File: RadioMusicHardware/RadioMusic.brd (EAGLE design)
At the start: 99 x 19.1 mm, 24 parts, among them IC1 TL074P, IC2 7805L, U1 USD-SOCKETNEW

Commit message: Output circuitry
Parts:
- added C3, C6: 1n, TomW:C050-024X044
- added C7, C8: 100n, TomW:C050-025X075
- added R3, R5, R6: 8.2k, TomW:0207/10
- added R4: 220R, TomW:0207/10
- added R7: 1k, TomW:0207/10
- added R8: 3.3K, TomW:0207/10
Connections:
- new net DAC: C8.2, U$1.RESET
- new net N$10: C8.1, R5.1
- new net N$2: C6.1, IC1.10, R3.2
- new net N$4: C3.2, R3.1, R5.2
- new net N$5: C3.1, C7.2, IC1.8, IC1.9
- new net N$6: C7.1, IC1.12, R6.2
- new net N$7: IC1.13, R7.2, R8.1
- new net N$8: IC1.14, R4.1, R8.2
- new net N$9: OUT1.P$3, R4.2
- net GND: now also C6.2, OUT1.P$1, R6.1, R7.1
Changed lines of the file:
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@@
 <layer number="97" name="Info" color="7" fill="1" visible="no" active="no"/>
 <layer number="98" name="Guide" color="6" fill="1" visible="no" active="no"/>
+<layer number="99" name="SpiceOrder" color="5" fill="1" visible="no" active="no"/>
 <layer number="100" name="Muster" color="7" fill="1" visible="no" active="no"/>
 <layer number="101" name="Patch_Top" color="12" fill="4" visible="yes" active="yes"/>
@@
 <element name="D1" library="diode" package="DO34-7" value="BAT81" x="4.445" y="-15.24"/>
 <element name="D2" library="diode" package="DO34-7" value="BAT81" x="4.445" y="-21.59"/>
+<element name="R3" library="TomW" package="0207/10" value="8.2k" x="4.445" y="-26.035"/>
+<element name="R4" library="TomW" package="0207/10" value="220R" x="4.445" y="-29.845"/>
+<element name="R5" library="TomW" package="0207/10" value="8.2k" x="4.445" y="-33.655"/>
+<element name="C3" library="TomW" package="C050-024X044" value="1n" x="1.905" y="-37.465"/>
+<element name="C6" library="TomW" package="C050-024X044" value="1n" x="1.905" y="-41.275"/>
+<element name="C7" library="TomW" package="C050-025X075" value="100n" x="2.54" y="-44.45"/>
+<element name="R6" library="TomW" package="0207/10" value="8.2k" x="4.445" y="-47.625"/>
+<element name="R7" library="TomW" package="0207/10" value="1k" x="4.445" y="-51.435"/>
+<element name="R8" library="TomW" package="0207/10" value="3.3K" x="4.445" y="-55.245"/>
+<element name="C8" library="TomW" package="C050-025X075" value="100n" x="2.54" y="-59.055"/>
 </elements>
 <signals>
@@
 <contactref element="D2" pad="A"/>
 <contactref element="CHANNEL" pad="1"/>
+<contactref element="OUT1" pad="P$1"/>
+<contactref element="C6" pad="2"/>
+<contactref element="R6" pad="1"/>
+<contactref element="R7" pad="1"/>
 <wire x1="92.075" y1="10.795" x2="94.615" y2="10.795" width="0" layer="19" extent="1-1"/>
 <wire x1="94.615" y1="8.255" x2="94.615" y2="10.795" width="0" layer="19" extent="1-1"/>
@@
 <wire x1="37.45" y1="6.39" x2="42.545" y2="9.525" width="0" layer="19" extent="1-1"/>
 <wire x1="27.435" y1="5.08" x2="37.45" y2="6.39" width="0" layer="19" extent="1-1"/>
-<wire x1="-0.635" y1="-10.16" x2="27.435" y2="5.08" width="0" layer="19" extent="1-1"/>
+<wire x1="12.83" y1="5.08" x2="27.435" y2="5.08" width="0" layer="19" extent="1-1"/>
+<wire x1="-0.635" y1="-10.16" x2="12.83" y2="5.08" width="0" layer="19" extent="1-1"/>
 <wire x1="8.255" y1="-21.59" x2="-0.635" y2="-10.16" width="0" layer="19" extent="1-1"/>
+<wire x1="4.445" y1="-41.275" x2="8.255" y2="-21.59" width="0" layer="19" extent="1-1"/>
+<wire x1="-0.635" y1="-47.625" x2="4.445" y2="-41.275" width="0" layer="19" extent="1-1"/>
+<wire x1="-0.635" y1="-51.435" x2="-0.635" y2="-47.625" width="0" layer="19" extent="1-1"/>
 </signal>
 <signal name="+12V" class="1">
@@
 <wire x1="37.45" y1="8.89" x2="67.945" y2="1.905" width="0" layer="19" extent="1-1"/>
 </signal>
+<signal name="DAC">
+<contactref element="U$1" pad="RESET"/>
+<contactref element="C8" pad="2"/>
+<wire x1="42.545" y1="4.445" x2="5.08" y2="-59.055" width="0" layer="19" extent="1-1"/>
+</signal>
+<signal name="N$2">
+<contactref element="IC1" pad="10"/>
+<contactref element="R3" pad="2"/>
+<contactref element="C6" pad="1"/>
+<wire x1="9.525" y1="-26.035" x2="29.845" y2="24.765" width="0" layer="19" extent="1-1"/>
+<wire x1="-0.635" y1="-41.275" x2="9.525" y2="-26.035" width="0" layer="19" extent="1-1"/>
+</signal>
+<signal name="N$4">
+<contactref element="R3" pad="1"/>
+<contactref element="R5" pad="2"/>
+<contactref element="C3" pad="2"/>
+<wire x1="9.525" y1="-33.655" x2="4.445" y2="-37.465" width="0" layer="19" extent="1-1"/>
+<wire x1="-0.635" y1="-26.035" x2="4.445" y2="-37.465" width="0" layer="19" extent="1-1"/>
+</signal>
+<signal name="N$5">
+<contactref element="C3" pad="1"/>
+<contactref element="IC1" pad="8"/>
+<contactref element="IC1" pad="9"/>
+<contactref element="C7" pad="2"/>
+<wire x1="24.765" y1="24.765" x2="27.305" y2="24.765" width="0" layer="19" extent="1-1"/>
+<wire x1="-0.635" y1="-37.465" x2="24.765" y2="24.765" width="0" layer="19" extent="1-1"/>
+<wire x1="5.08" y1="-44.45" x2="-0.635" y2="-37.465" width="0" layer="19" extent="1-1"/>
+</signal>
+<signal name="N$6">
+<contactref element="C7" pad="1"/>
+<contactref element="IC1" pad="12"/>
+<contactref element="R6" pad="2"/>
+<wire x1="9.525" y1="-47.625" x2="34.925" y2="24.765" width="0" layer="19" extent="1-1"/>
+<wire x1="0" y1="-44.45" x2="9.525" y2="-47.625" width="0" layer="19" extent="1-1"/>
+</signal>
+<signal name="N$7">
+<contactref element="IC1" pad="13"/>
+<contactref element="R7" pad="2"/>
+<contactref element="R8" pad="1"/>
+<wire x1="9.525" y1="-51.435" x2="37.465" y2="24.765" width="0" layer="19" extent="1-1"/>
+<wire x1="-0.635" y1="-55.245" x2="9.525" y2="-51.435" width="0" layer="19" extent="1-1"/>
+</signal>
+<signal name="N$8">
+<contactref element="IC1" pad="14"/>
+<contactref element="R4" pad="1"/>
+<contactref element="R8" pad="2"/>
+<wire x1="-0.635" y1="-29.845" x2="40.005" y2="24.765" width="0" layer="19" extent="1-1"/>
+<wire x1="9.525" y1="-55.245" x2="-0.635" y2="-29.845" width="0" layer="19" extent="1-1"/>
+</signal>
+<signal name="N$9">
+<contactref element="R4" pad="2"/>
+<contactref element="OUT1" pad="P$3"/>
+<wire x1="1.51" y1="5.08" x2="9.525" y2="-29.845" width="0" layer="19" extent="1-1"/>
+</signal>
+<signal name="N$10">
+<contactref element="R5" pad="1"/>
+<contactref element="C8" pad="1"/>
+<wire x1="-0.635" y1="-33.655" x2="0" y2="-59.055" width="0" layer="19" extent="1-1"/>
+</signal>
 </signals>

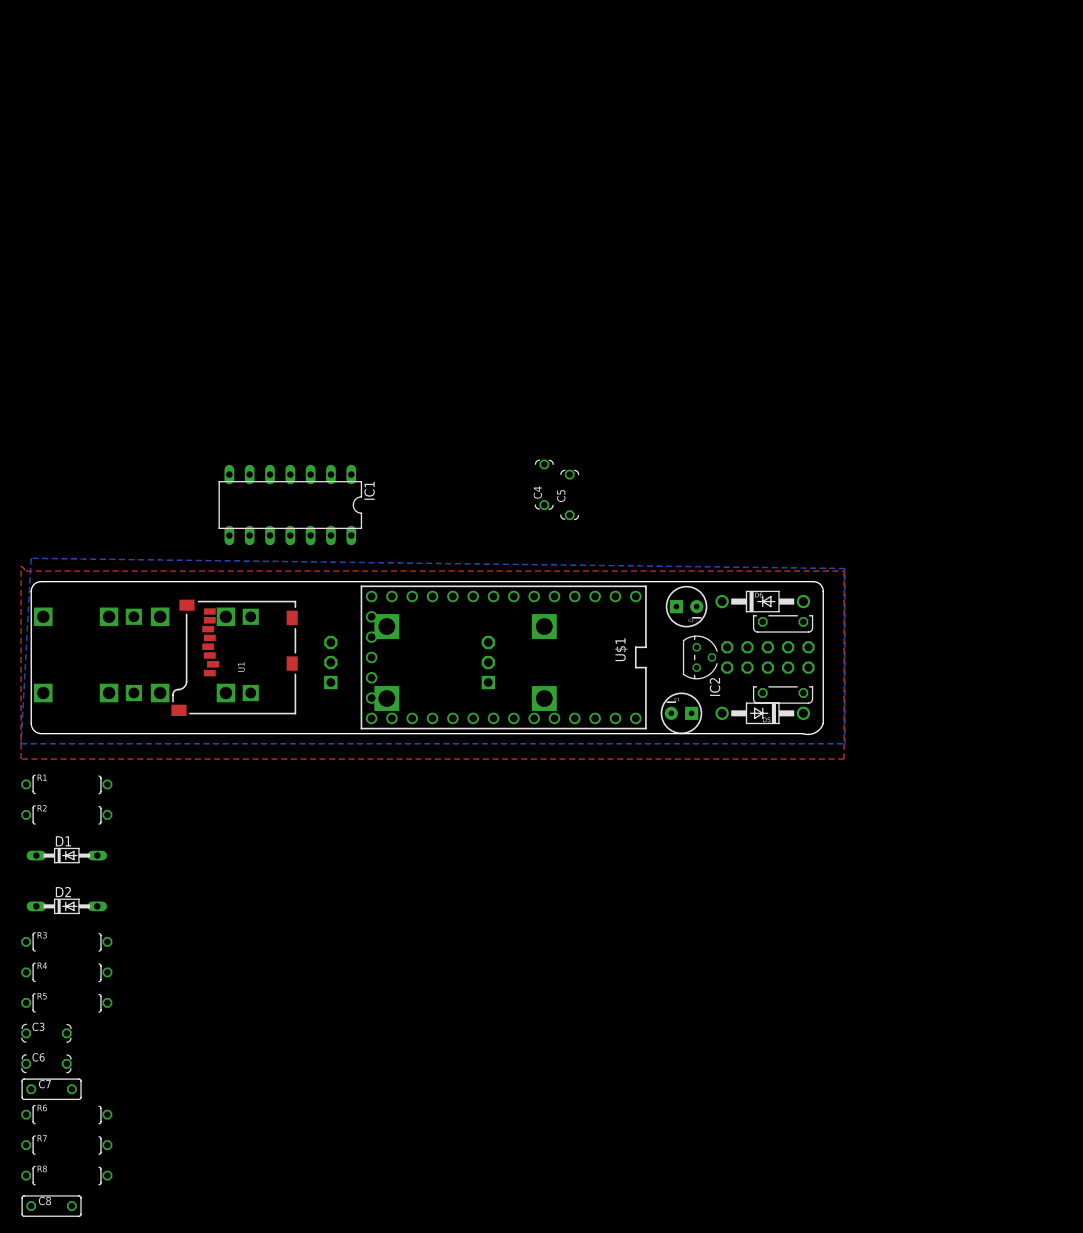
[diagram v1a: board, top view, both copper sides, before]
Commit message: Basic hardware schematic complete
Only needs SD connections & checking
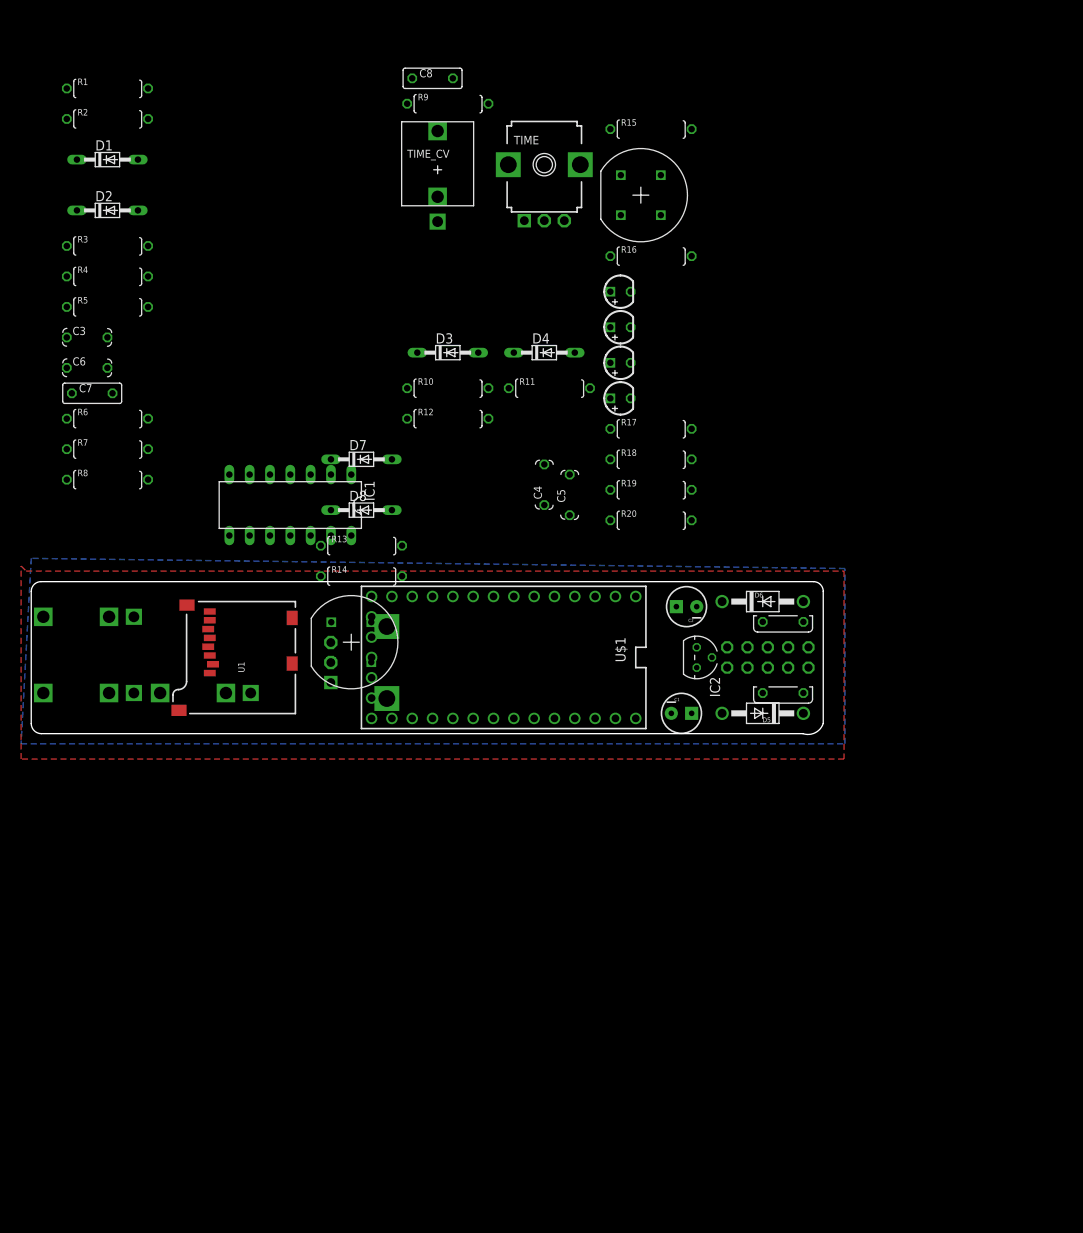
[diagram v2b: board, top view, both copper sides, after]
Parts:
- removed CV2: THONKICONN, TomW:THONKICONN
- removed GAIN1: 50k, TomW:EVUF
- added BANK_BUTTON, RESET_BUTTON: (no value), TomW:D6_BUTTON_RND
- added D3, D4, D7, D8: BAT81, diode:DO34-7
- added LED1, LED2, LED3, LED4: (no value), TomW:LED3MM
- added R10, R13: 100k, TomW:0207/10
- added R11: 200k, TomW:0207/10
- added R12, R9: 47R, TomW:0207/10
- added R14: 220R, TomW:0207/10
- added R15, R16: 10k, TomW:0207/10
- added R17, R18, R19, R20: 1k, TomW:0207/10
- added TIME: 50k, TomW:EVUF
- added TIME_CV: THONKICONN, TomW:THONKICONN
- R1: value 10k -> 100k
- R2: value 10k -> 200k
- moved C8 148.8 mm to (50.2, 81.9)
- moved C3 87.1 mm to (6.99, 49.5)
- moved C6 87.1 mm to (6.99, 45.7)
- moved C7 87.1 mm to (7.62, 42.5)
- moved D2 87.1 mm to (9.53, 65.4)
- moved R3 87.1 mm to (9.53, 61.0)
- moved R4 87.1 mm to (9.53, 57.1)
- moved R5 87.1 mm to (9.53, 53.3)
- moved R6 87.1 mm to (9.53, 39.4)
- moved R7 87.1 mm to (9.53, 35.6)
- moved R8 87.1 mm to (9.53, 31.8)
- moved D1 87.1 mm to (9.53, 71.8)
- moved R1 87.1 mm to (9.53, 80.6)
- moved R2 87.1 mm to (9.53, 76.8)
- renumbered OUT2 to RESET
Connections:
- new net N$11: R10.1, R11.2, TIME_CV.P$3
- new net N$12: IC1.5, R10.2
- new net N$13: LED1.A, U$1.3
- new net N$14: R14.1, RESET.P$3
- new net N$15: LED2.A, U$1.4
- new net N$16: LED3.A, U$1.5
- new net N$17: LED4.A, U$1.6
- new net N$18: LED1.K, R17.2
- new net N$19: LED2.K, R18.2
- new net N$20: LED3.K, R19.2
- new net N$21: LED4.K, R20.2
- new net PIN2: BANK_BUTTON.P$1, BANK_BUTTON.P$2, R15.2, U$1.2
- new net PIN20/A6: D3.A, D4.C, R12.2, U$1.20/A6
- new net PIN21/A7: TIME.2, U$1.21/A7
- new net PIN8: R16.2, RESET_BUTTON.P$1, RESET_BUTTON.P$2, U$1.8
- new net PIN9: D7.A, D8.C, R13.2, R14.2, U$1.9
- net +3.3V: now also BANK_BUTTON.P$3, BANK_BUTTON.P$4, D3.C, D7.C, RESET_BUTTON.P$3, RESET_BUTTON.P$4, TIME.3
- net GND: now also D4.A, D8.A, R11.1, R13.1, R15.1, R16.1, R17.1, R18.1, R19.1, R20.1, RESET.P$1, TIME.1, TIME_CV.P$1, U1.CD1, U1.CD2, U1.GND1, U1.GND3
- net PIN22/A8: now also IC1.6, IC1.7, R12.1, R9.1, R9.2

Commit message: Starting PCB layout
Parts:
- removed U1: USD-SOCKETNEW, SparkFun-Connectors:MICRO-SD-SOCKET-PP
- added L1, L2: BL01RN1A, inductors:BL01RN1A
- added U$3: VERT_SD_CARD, TomW:VERT_MICROSD
- BANK_BUTTON, RESET_BUTTON: value (none) -> D6_PUSH_SWITCH
- CHANNEL_CV, OUT1, RESET, TIME_CV: value THONKICONN -> WQP-PJ301M-12_JACK; device TomW:THONKICONN -> thonkiconn:WQP-PJ301M-12_JACK
- U$1: value TEENSY_3.0_BASIC -> TEENSY_3.1_TW; device Teensy3.0:TEENSY_3.0_BASIC -> TomW:TEENSY_3.1_TW
- moved BANK_BUTTON 78.8 mm to (71.1, 83.8)
- moved RESET_BUTTON 72.2 mm to (37.5, 6.35)
- moved TIME_CV 63.4 mm to (21.0, 14.6), turned to 90 degrees
- moved TIME 62.1 mm to (55.9, 9.53), turned to 270 degrees
- moved U$1 49.9 mm to (19.1, 39.4), flipped to the bottom
- moved R13 48.4 mm to (37.5, 71.8)
- moved R14 48.4 mm to (38.1, 67.9)
- moved U$2 47.9 mm to (119.4, -2.29)
- moved D8 47.8 mm to (36.8, 75.6)
- moved D7 46.0 mm to (36.2, 80.0)
- moved LED1 45.6 mm to (97.8, 16.5)
- moved LED2 45.6 mm to (97.8, 12.1)
- moved LED3 45.6 mm to (97.8, 7.62)
- moved LED4 45.6 mm to (97.8, 3.17)
- moved R20 39.5 mm to (55.9, 59.7)
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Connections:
- removed net VBAT: U$1.VBAT
- new net MISO: U$1.12, U$3.P$7
- new net MOSI: U$1.7, U$3.P$3
- new net N$22: 1.2, L1.1
- new net N$23: FUSE.2, L2.1
- new net SCLK: U$1.14/A0, U$3.P$5
- new net SS: U$1.10, U$3.P$2
- net +12V: now also L1.2; no longer 1.2
- net +3.3V: now also U$3.P$4; no longer U$1.3.3V1
- net -12V: now also L2.2; no longer FUSE.2
- net DAC: now also U$1.DAC; no longer U$1.RESET
- net GND: now also CHANNEL_CV.P$3, OUT1.P$3, RESET.P$3, TIME_CV.P$3, U$3.GND1, U$3.GND2, U$3.P$6; no longer CHANNEL_CV.P$1, OUT1.P$1, RESET.P$1, TIME_CV.P$1, U$1.GND1, U1.CD1, U1.CD2, U1.GND1, U1.GND3
- net N$1: now also CHANNEL_CV.P$1; no longer CHANNEL_CV.P$3
- net N$11: now also TIME_CV.P$1; no longer TIME_CV.P$3
- net N$14: now also RESET.P$1; no longer RESET.P$3
- net N$9: now also OUT1.P$1; no longer OUT1.P$3
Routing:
- removed copper zone on layer 1, net GND
- removed copper zone on layer 16, net GND
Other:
- board size 99 x 19.1 mm -> 100 x 49 mm
